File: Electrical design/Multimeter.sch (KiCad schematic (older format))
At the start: 39 parts, among them P101 CONN_02X07, P102 CONN_01X06, P103 Mounting hole, P104 Mounting hole, P105 Mounting hole, Q101 Q_PMOS_GSD, Q102 Q_NMOS_GSD, U101 STM32F373R8Tx, U102 ILI9341_LCD_Breakout, U103 BD4835, Y101 8 MHz

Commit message: Add documentation. Fix some issues found while writing it.
The issues fixed:
Change R245-246 to 1M.
Remove D211-212 and add D213-214.
Power the analog switches from +V_int.
Reconfigure range combination jumpers.
Remove "GND" net.
Correct values of C103-105, and add R106-108 (correcting values of R101-103).
Change +V_int around to be based of +3.3VA instead of +BATT, and clamp to 3.5 V.
Along with above, remove GND rail, mostly replacing with GNDA.
Update PCB for changes.
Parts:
- added R106, R107, R108: 500R, my footprints:SMDuniversal_0603to1210_HandSoldering, symbol R
- C103, C104, C105: value 0.22u -> 3.9n
- P101: value CONN_02X07 -> Expansion header
- P102: value CONN_01X06 -> Programming header
- R101, R102, R103: value 1k -> 500R
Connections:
- net at C117.2, C120.1, Q102.3 (D)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: now also U102.4 (Reset)
- removed net COMMON: C103.2, C104.2, C105.2, P101.11 (P11), U101.27 (ADC1_IN9/SDADC1_AIN5P/SDADC1_AIN6M/TIM3_CH4/TSC_G3_IO4/PB1), U101.30 (PE9/DAC1_EXTI9/DAC2_EXTI9/SDADC1_AIN7P/SDADC1_AIN8M/SDADC2_AIN7P/SDADC2_AIN8M), U101.35 (ADC1_EXTI15/I2S2_SD/RTC_REFIN/SDADC1_EXTI15/SDADC2_EXTI15/SDADC3_AIN7P/SDADC3_AIN8M/SDADC3_EXTI15/SPI2_MOSI/TIM12_CH2/TIM15_CH1N/TIM15_CH2/TSC_G6_IO2/PB15)
- new net COMMON_Io: C105.2, R106.1, U101.35 (ADC1_EXTI15/I2S2_SD/RTC_REFIN/SDADC1_EXTI15/SDADC2_EXTI15/SDADC3_AIN7P/SDADC3_AIN8M/SDADC3_EXTI15/SPI2_MOSI/TIM12_CH2/TIM15_CH1N/TIM15_CH2/TSC_G6_IO2/PB15)
- new net COMMON_LV: C103.2, R108.1, U101.30 (PE9/DAC1_EXTI9/DAC2_EXTI9/SDADC1_AIN7P/SDADC1_AIN8M/SDADC2_AIN7P/SDADC2_AIN8M)
- new net COMMON_V: C104.2, R107.1, U101.27 (ADC1_IN9/SDADC1_AIN5P/SDADC1_AIN6M/TIM3_CH4/TSC_G3_IO4/PB1)
- new net Main Input / Output/COMMON: P101.11 (P11), R106.2, R107.2, R108.2
- no-connect marks 4 -> 3
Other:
- moved on the sheet: C101, C102, C103, C104, C105, C106, C107, C108, C109, C110, C111, C112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

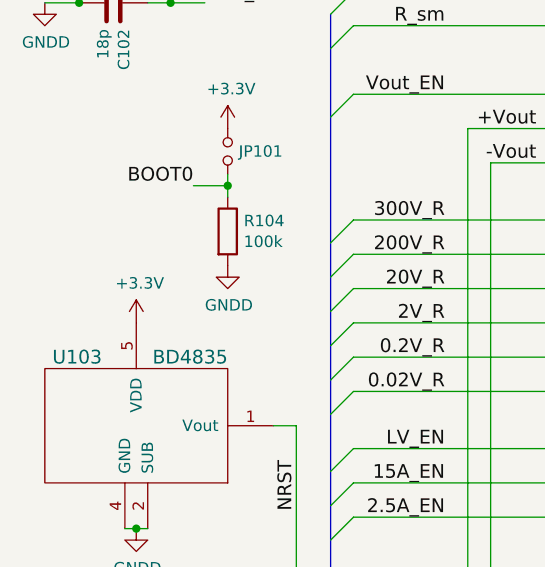
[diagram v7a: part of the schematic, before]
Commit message: Connect the reset circuit to +BATT so that it actually works!
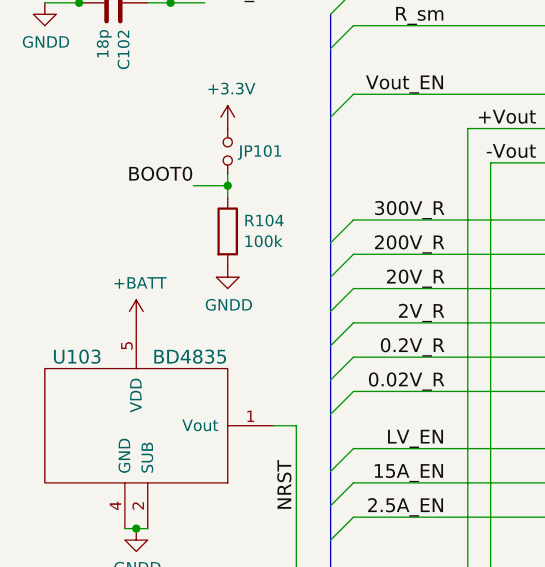
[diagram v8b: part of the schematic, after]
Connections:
- net +3V3: no longer U103.5 (VDD)
- new net +BATT: U103.5 (VDD)
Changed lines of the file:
@@
 Sheet 1 5
 Title "Multimeter – Overview"
-Date "2016-07-14"
-Rev "0.8"
+Date "2016-08-15"
+Rev "0.9"
 Comp ""
 Comment1 "Licensed under the GNU GPL v3"
@@
 $EndComp
 $Comp
-L +3.3V #PWR107
-U 1 1 576110F8
-P 950 2600
-F 0 "#PWR107" H 950 2450 50  0001 C CNN
-F 1 "+3.3V" H 965 2773 50  0000 C CNN
-F 2 "" H 950 2600 50  0000 C CNN
-F 3 "" H 950 2600 50  0000 C CNN
-	1    950  2600
-	1    0    0    -1
-$EndComp
-$Comp
 L GNDD #PWR110
 U 1 1 5761132F
@@
 Connection ~ 8600 2200
 Connection ~ 9000 2100
+$Comp
+L +BATT #PWR?
+U 1 1 57B0FC16
+P 950 2600
+F 0 "#PWR?" H 950 2450 50  0001 C CNN
+F 1 "+BATT" H 965 2773 50  0000 C CNN
+F 2 "" H 950 2600 50  0000 C CNN
+F 3 "" H 950 2600 50  0000 C CNN
+	1    950  2600
+	1    0    0    -1
+$EndComp
 $EndSCHEMATC
